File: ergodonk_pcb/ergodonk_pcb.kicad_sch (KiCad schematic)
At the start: 133 parts, among them J10 TRRS Double Sided, J12 Conn_01x04_Socket, Q1 TIP120, SW08_RH10 SW_PUSH_LED, SW1 SW_PUSH_LED, SW10 SW_PUSH_LED, SW11 SW_PUSH_LED, SW12 SW_PUSH_LED, SW13 SW_PUSH_LED, SW14 SW_PUSH_LED, SW15 SW_PUSH_LED, SW16 SW_PUSH_LED, SW17 SW_PUSH_LED, SW18_RH10 SW_PUSH_LED, SW2 SW_PUSH_LED, SW20 SW_PUSH_LED, SW21 SW_PUSH_LED, SW22 SW_PUSH_LED, SW23 SW_PUSH_LED, SW24 SW_PUSH_LED, SW25 SW_PUSH_LED, SW26 SW_PUSH_LED, SW27 SW_PUSH_LED, SW28_RH10 SW_PUSH_LED, SW3 SW_PUSH_LED, SW30 SW_PUSH_LED, SW31 SW_PUSH_LED, SW32 SW_PUSH_LED, SW33 SW_PUSH_LED, SW34 SW_PUSH_LED, SW35 SW_PUSH_LED, SW36 SW_PUSH_LED, SW37 SW_PUSH_LED, SW38_RH10 SW_PUSH_LED, SW4 SW_PUSH_LED, SW40 SW_PUSH_LED, SW42 SW_PUSH_LED, SW43 SW_PUSH_LED, SW44 SW_PUSH_LED, SW45 SW_PUSH_LED, SW46 SW_PUSH_LED, SW47 SW_PUSH_LED, SW48_RH10 SW_PUSH_LED, SW5 SW_PUSH_LED, SW50 SW_PUSH_LED, SW51 SW_PUSH_LED, SW52 SW_PUSH_LED, SW53 SW_PUSH_LED, SW54 SW_PUSH_LED, SW55 SW_PUSH_LED, SW56 SW_PUSH_LED, SW57 SW_PUSH_LED, SW58 SW_PUSH_LED, SW6 SW_PUSH_LED, SW7 SW_PUSH_LED, U10 Pico

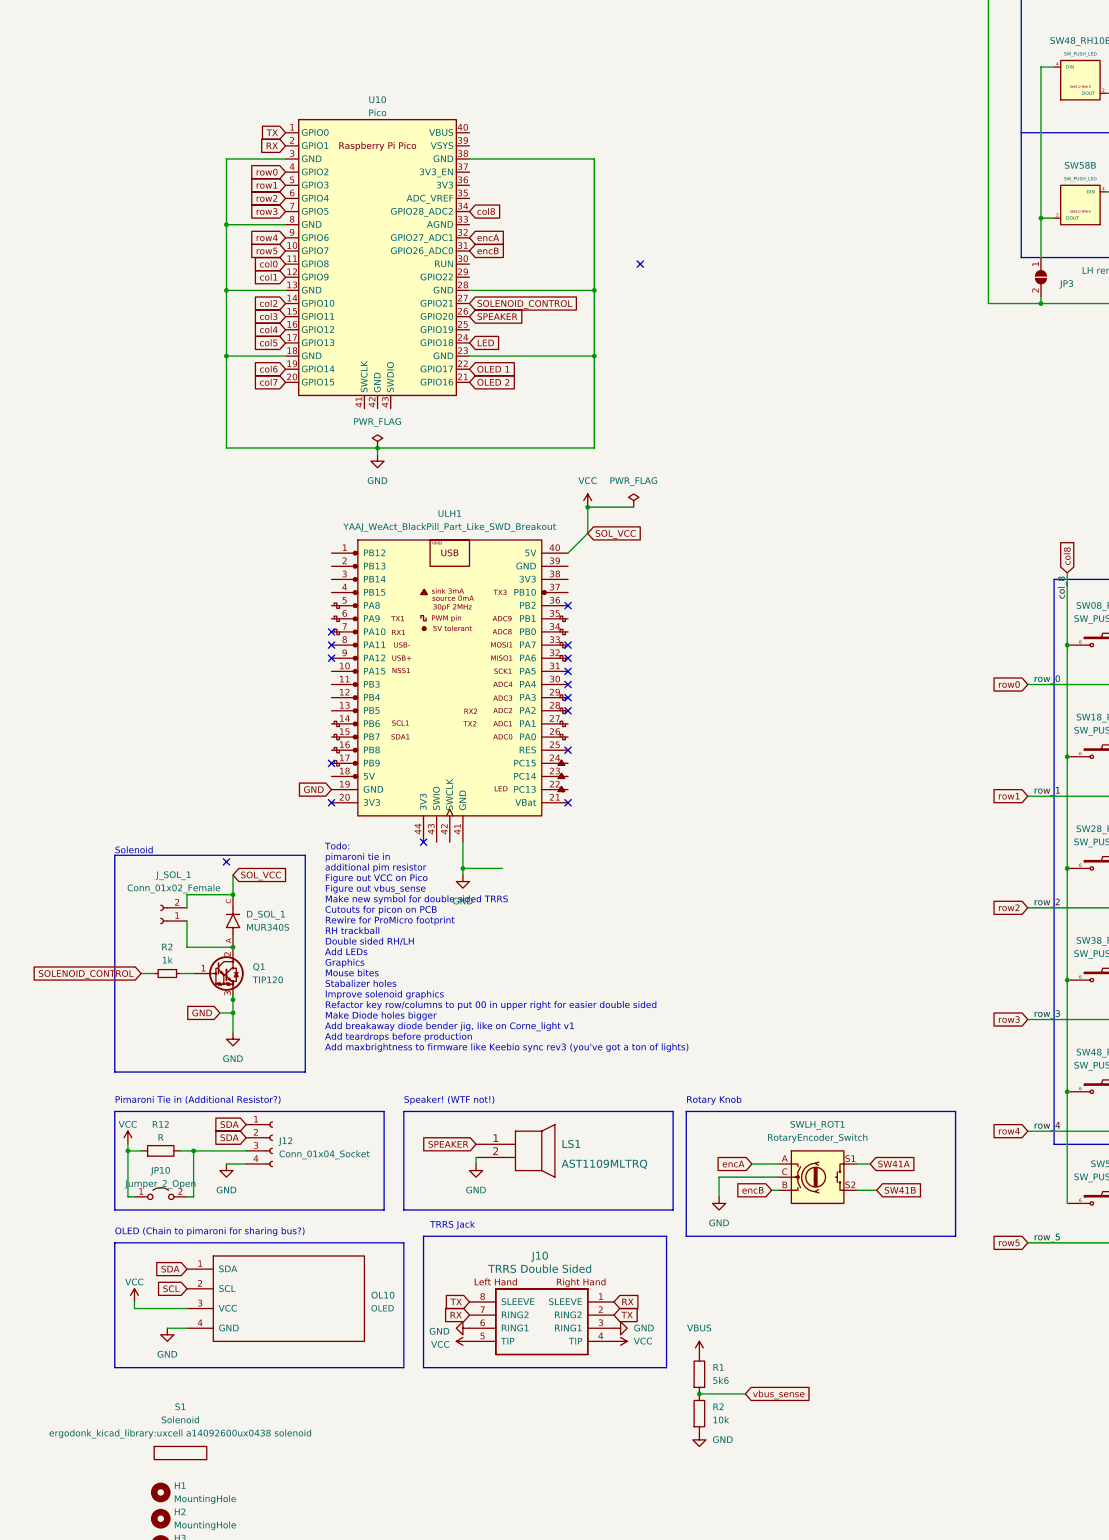
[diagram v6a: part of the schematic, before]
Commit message: Removed blackpill from schematic and pcb Updated pico placement Updated outline source for Inkscape regeneration
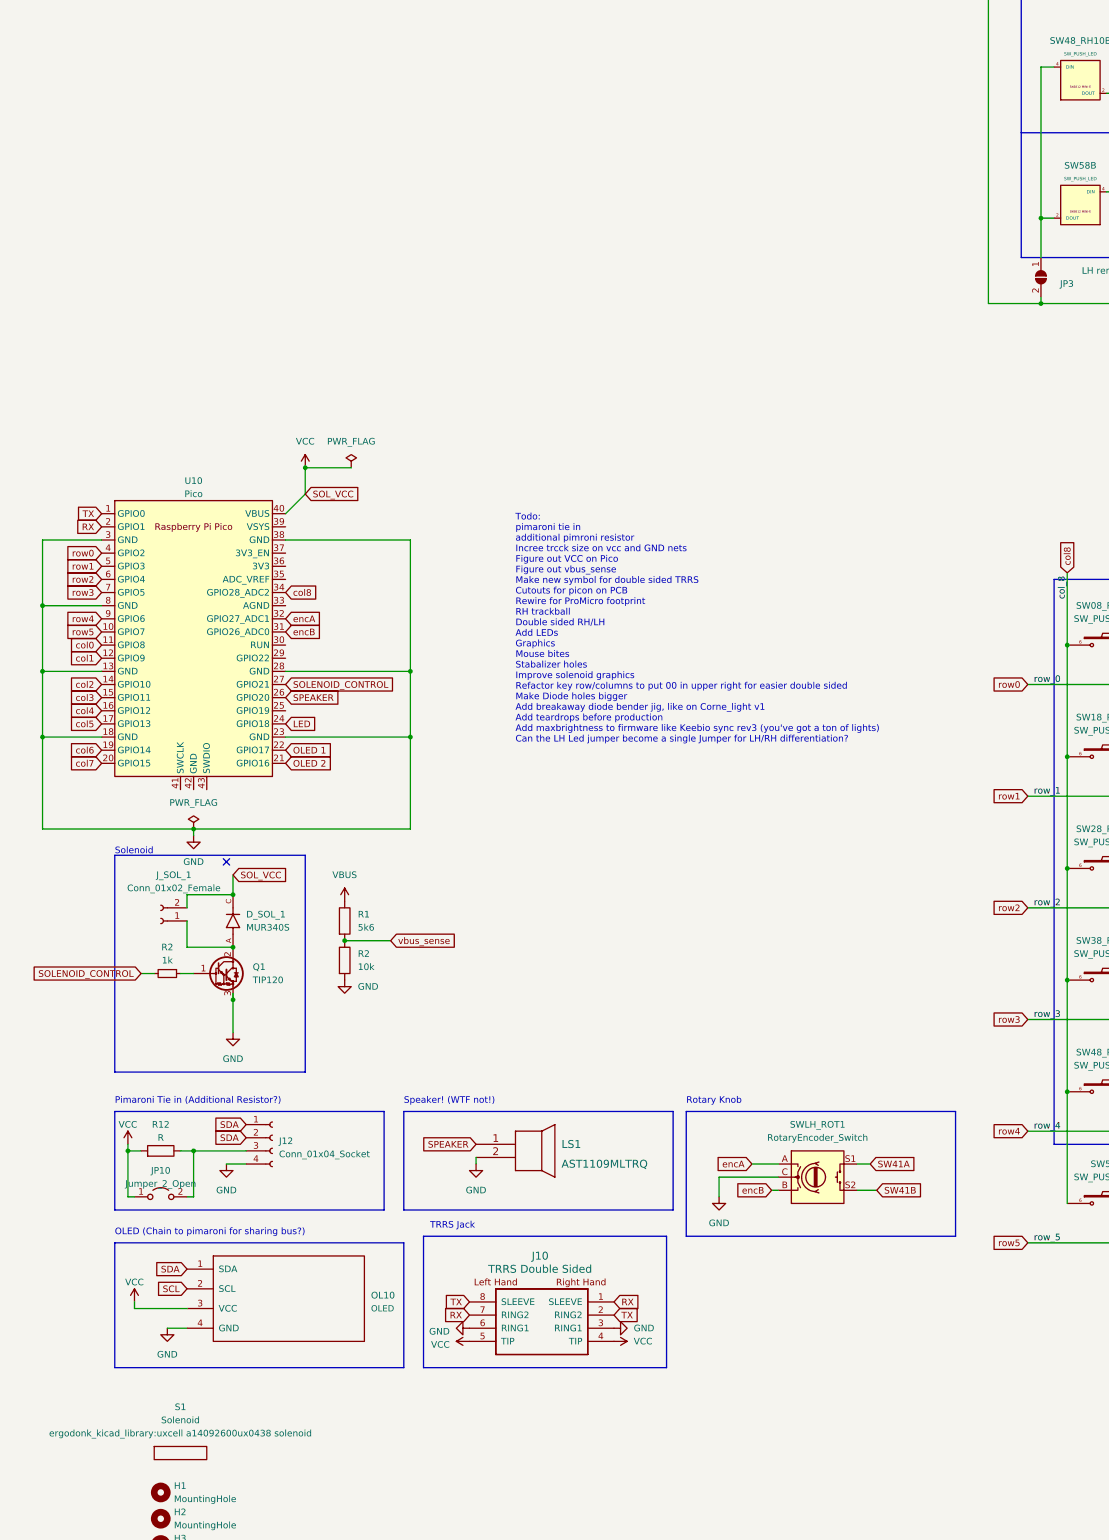
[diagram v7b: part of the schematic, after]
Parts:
- removed ULH1: YAAJ_WeAct_BlackPill_Part_Like_SWD_Breakout, Footprints:YAAJ_WeAct_BlackPill_SWD_2, symbol YAAJ_WeAct_BlackPill_Part_Like_SWD_Breakout:YAAJ_WeAct_BlackPill_Part_Like_SWD_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
- U10: footprint RPi_Pico:RPi_Pico_SMD_TH -> MCU_RaspberryPi_and_Boards:RPi_Pico_SMD_TH
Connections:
- net VCC: now also U10.40 (VBUS)
- no-connect marks 17 -> 1
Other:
- note added: "Todo: pimaroni tie in additional pimroni resistor Incree trcck size on vcc and GND nets Figure out VCC on Pico Figure out vbus_sense Make new symbol for double sided TRRS Cutouts for picon on PCB Rewire for ProMicro footprint RH trackball Double sided RH/LH Add LEDs Graphics Mouse bites Stabalizer holes Improve solenoid graphics Refactor key row/columns to put 00 in upper right for easier double 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"
- note removed: "Todo: pimaroni tie in additional pim resistor Figure out VCC on Pico Figure out vbus_sense Make new symbol for double sided TRRS Cutouts for picon on PCB Rewire for ProMicro footprint RH trackball Double sided RH/LH Add LEDs Graphics Mouse bites Stabalizer holes Improve solenoid graphics Refactor key row/columns to put 00 in upper right for easier double sided Make Diode holes bigger Add breakawa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"
- moved on the sheet: R1, R2, U10

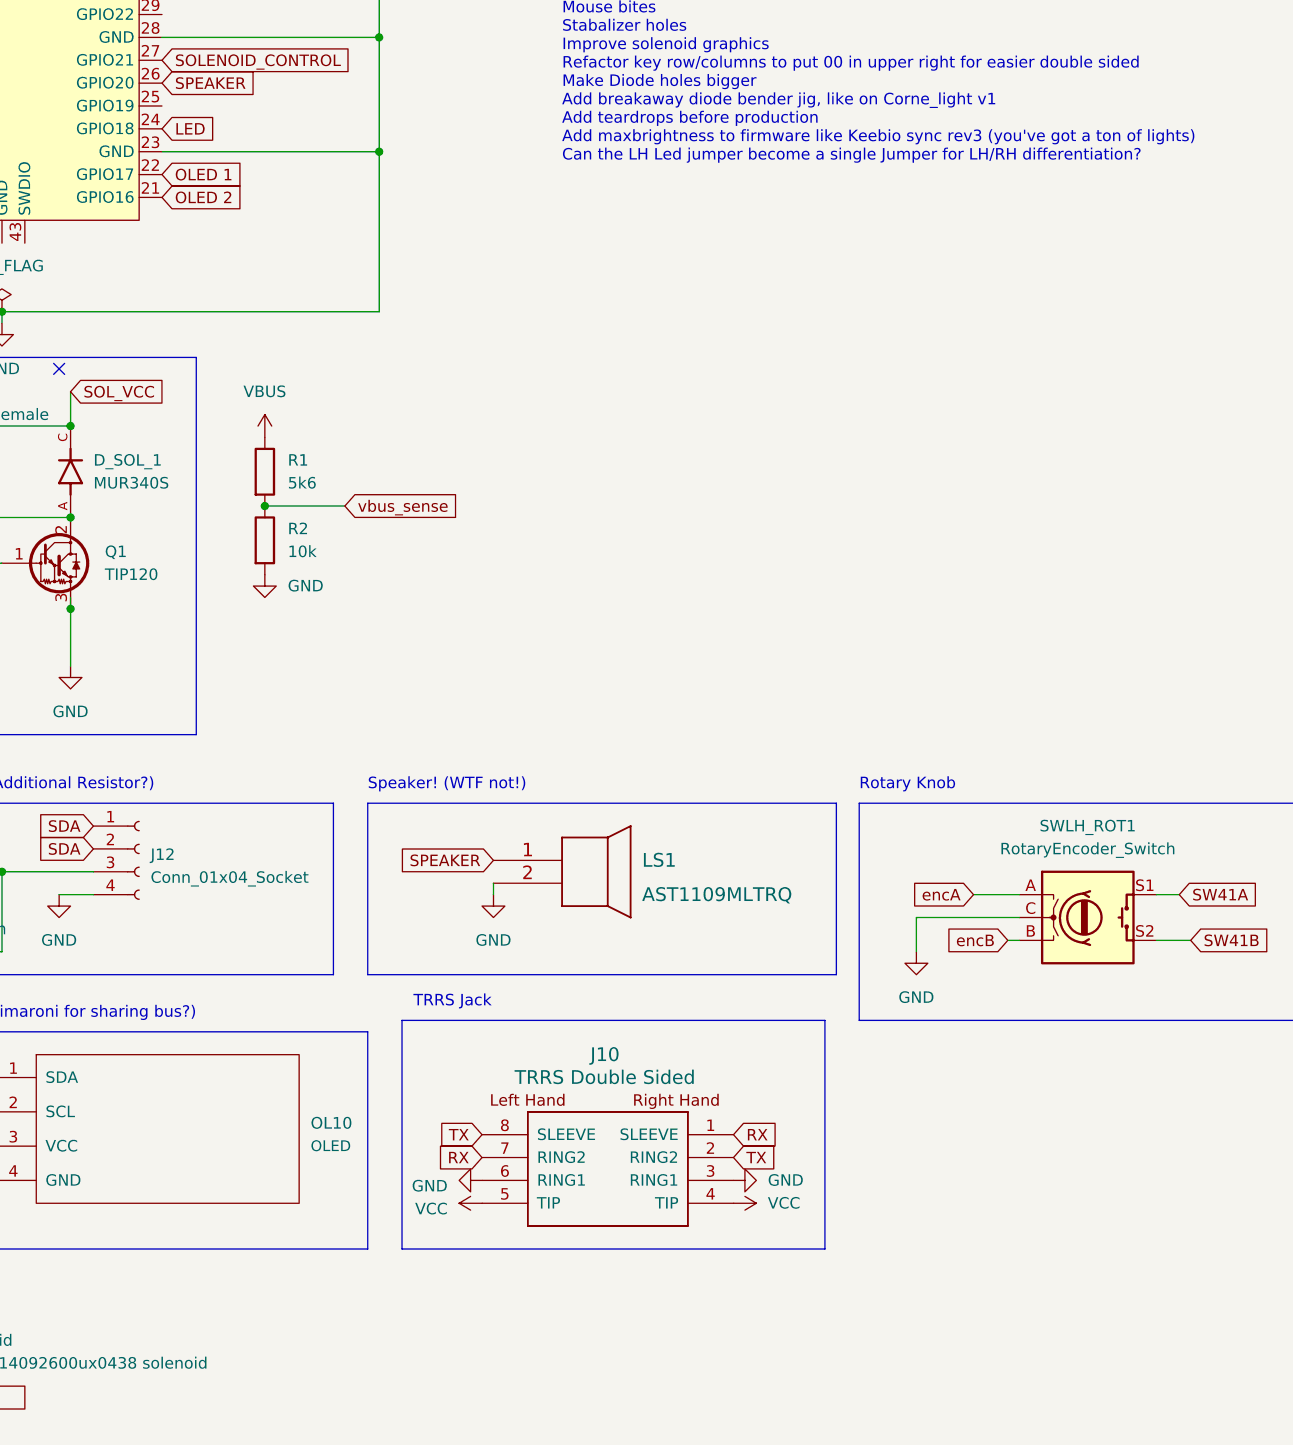
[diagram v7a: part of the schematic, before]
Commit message: Added pimaroni rough symbol
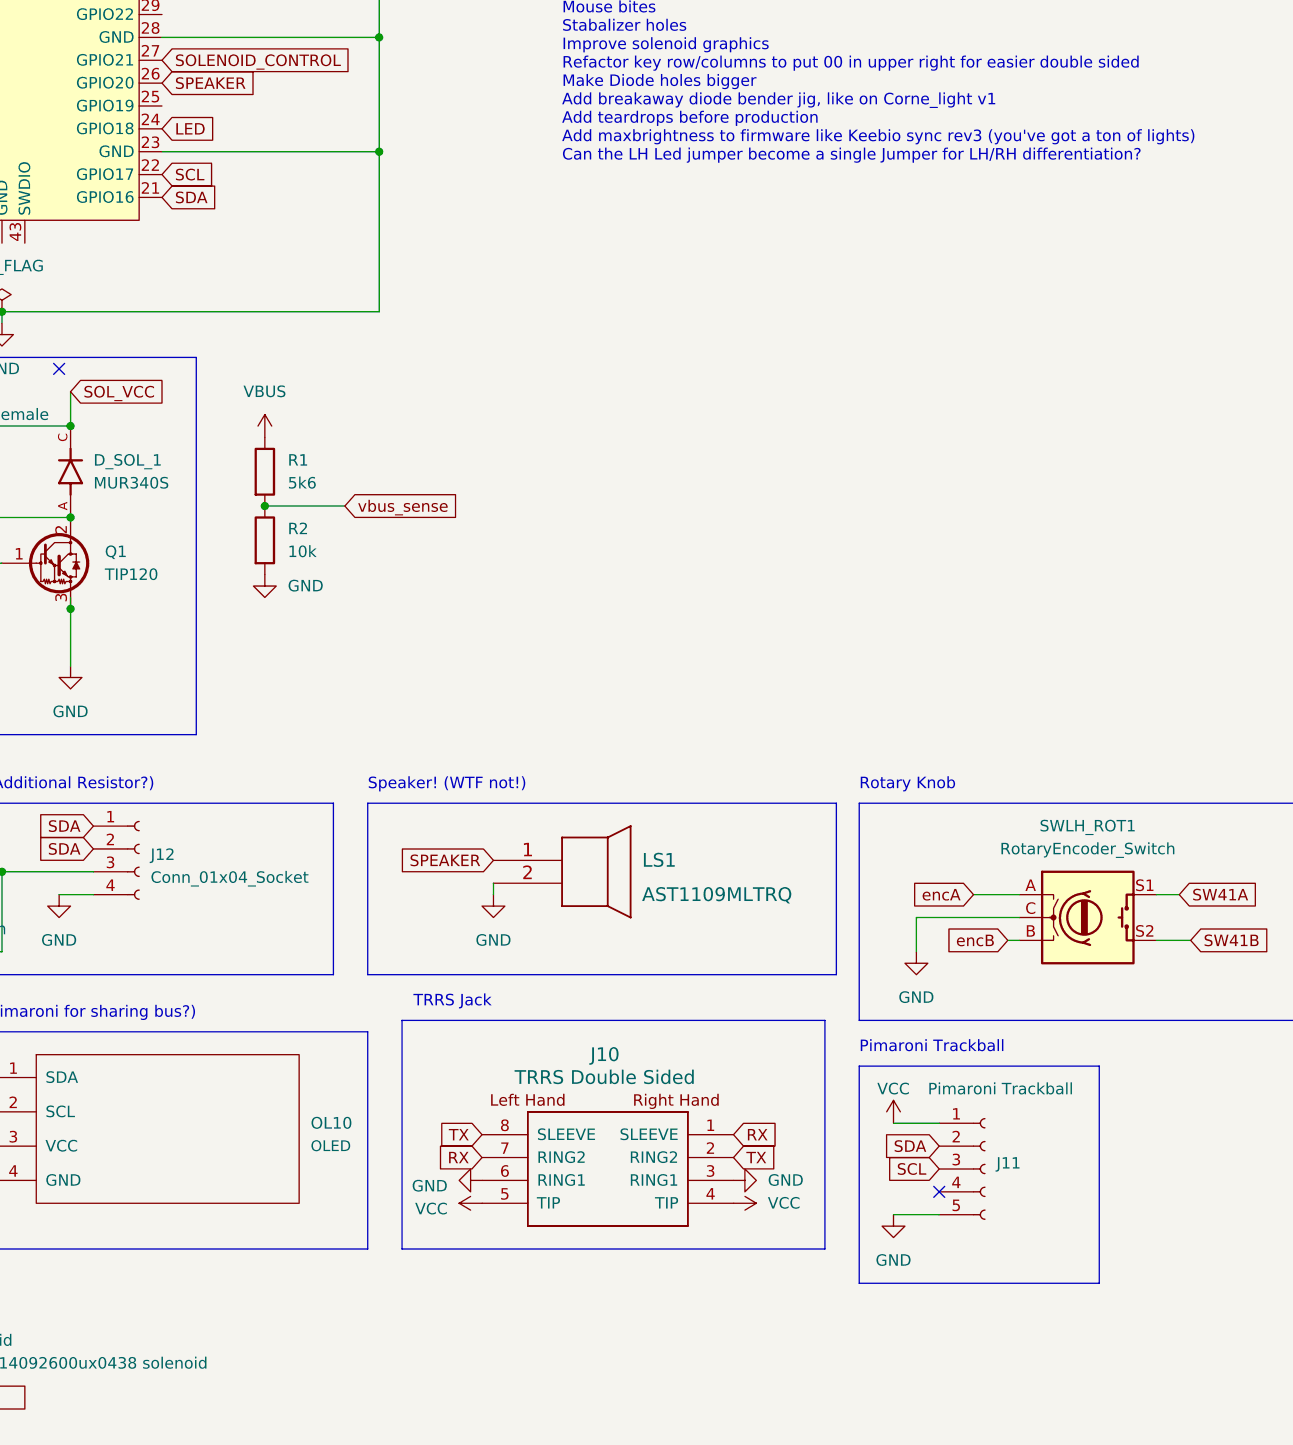
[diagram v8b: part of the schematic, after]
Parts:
- added J11: Pimaroni Trackball, ergodonk_kicad_library:pimoroni_trackball, symbol Connector:Conn_01x05_Socket
- OL10: footprint (none) -> ergodonk_kicad_library:OLED 128x64 Double sided
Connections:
- net OLED 1 is gone; now on net SCL: U10.22 (GPIO17)
- net OLED 2 is gone; now on net SDA: U10.21 (GPIO16)
- net GND: now also J11.5 (Pin_5)
- net SCL: now also J11.3 (Pin_3)
- net SDA: now also J11.2 (Pin_2)
- net VCC: now also J11.1 (Pin_1)
- no-connect marks 1 -> 2
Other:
- note added: "Pimaroni Trackball"
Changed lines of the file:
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@@
   )
   (no_connect (at 50.8 87.63))
+  (no_connect (at 148.59 179.07))
   (wire (pts (xy 50.8 146.05) (xy 54.61 146.05))
     (stroke (width 0) (type default))
@@
     (stroke (width 0) (type default))
   )
+  (wire (pts (xy 143.51 171.45) (xy 148.59 171.45))
+    (stroke (width 0) (type default))
+  )
   (wire (pts (xy 44.45 143.51) (xy 44.45 152.4))
     (stroke (width 0) (type default))
@@
     (stroke (width 0) (type default))
   )
+  (wire (pts (xy 143.51 181.61) (xy 148.59 181.61))
+    (stroke (width 0) (type default))
+  )
   (wire (pts (xy 384.81 -104.14) (xy 382.27 -104.14))
     (stroke (width 0) (type default))
@@
     (fill (type none))
   )
+  (rectangle (start 139.7 165.1) (end 166.37 189.23)
+    (stroke (width 0) (type default))
+    (fill (type none))
+  )
   (image (at 248.92 214.63) (scale 1.76046)
     (data
@@
     (effects (font (size 1.27 1.27)) (justify left bottom))
   )
+  (text "Pimaroni Trackball\n" (at 139.7 163.83 0)
+    (effects (font (size 1.27 1.27)) (justify left bottom))
+  )
   (text "Solenoid" (at 29.21 86.36 0)
     (effects (font (size 1.27 1.27)) (justify left bottom))
@@
     )
   )
+  (global_label "SCL" (shape input) (at 148.59 176.53 180) (fields_autoplaced)
+    (effects (font (size 1.27 1.27)) (justify right))
+    (property "Intersheetrefs" "${INTERSHEET_REFS}" (at 142.1766 176.53 0)
+      (effects (font (size 1.27 1.27)) (justify right) hide)
+    )
+  )
   (global_label "encB" (shape input) (at 62.23 43.18 0) (fields_autoplaced)
     (effects (font (size 1.27 1.27)) (justify left))
@@
     )
   )
+  (global_label "SDA" (shape input) (at 148.59 173.99 180) (fields_autoplaced)
+    (effects (font (size 1.27 1.27)) (justify right))
+    (property "Intersheetrefs" "${INTERSHEET_REFS}" (at 142.1161 173.99 0)
+      (effects (font (size 1.27 1.27)) (justify right) hide)
+    )
+  )
   (global_label "col5" (shape input) (at 26.67 60.96 180) (fields_autoplaced)
     (effects (font (size 1.27 1.27)) (justify right))
@@
     )
   )
-  (global_label "OLED 1" (shape input) (at 62.23 66.04 0) (fields_autoplaced)
+  (global_label "SCL" (shape input) (at 62.23 66.04 0) (fields_autoplaced)
     (effects (font (size 1.27 1.27)) (justify left))
-    (property "Intersheetrefs" "${INTERSHEET_REFS}" (at 71.8849 66.04 0)
+    (property "Intersheetrefs" "${INTERSHEET_REFS}" (at 68.6434 66.04 0)
       (effects (font (size 1.27 1.27)) (justify left) hide)
     )
@@
     )
   )
-  (global_label "OLED 2" (shape input) (at 62.23 68.58 0) (fields_autoplaced)
+  (global_label "SDA" (shape input) (at 62.23 68.58 0) (fields_autoplaced)
     (effects (font (size 1.27 1.27)) (justify left))
-    (property "Intersheetrefs" "${INTERSHEET_REFS}" (at 71.8849 68.58 0)
+    (property "Intersheetrefs" "${INTERSHEET_REFS}" (at 68.7039 68.58 0)
       (effects (font (size 1.27 1.27)) (justify left) hide)
     )
@@
     )
   )
+  (symbol (lib_name "VCC_1") (lib_id "power:VCC") (at 143.51 171.45 0) (unit 1)
+    (in_bom yes) (on_board yes) (dnp no)
+    (property "Reference" "#PWR022" (at 143.51 175.26 0)
+      (effects (font (size 1.27 1.27)) hide)
+    )
+    (property "Value" "VCC" (at 143.51 167.64 0)
+      (effects (font (size 1.27 1.27)))
+    )
+    (property "Footprint" "" (at 143.51 171.45 0)
+      (effects (font (size 1.27 1.27)) hide)
+    )
+    (property "Datasheet" "" (at 143.51 171.45 0)
+      (effects (font (size 1.27 1.27)) hide)
+    )
+    (pin "1")
+    (instances
+      (project "ergodonk_pcb"
+        (path "/ed1aaf15-4e1f-4159-b371-d99b3fb972ad"
+          (reference "#PWR022") (unit 1)
+        )
+      )
+    )
+  )
   (symbol (lib_id "SofleKeyboard:SW_PUSH_LED") (at 215.9 -63.5 0) (mirror y) (unit 2)
     (in_bom yes) (on_board yes) (dnp no)
@@
     )
   )
+  (symbol (lib_id "Connector:Conn_01x05_Socket") (at 153.67 176.53 0) (unit 1)
+    (in_bom yes) (on_board yes) (dnp no)
+    (property "Reference" "J11" (at 154.94 175.895 0)
+      (effects (font (size 1.27 1.27)) (justify left))
+    )
+    (property "Value" "Pimaroni Trackball" (at 147.32 167.64 0)
+      (effects (font (size 1.27 1.27)) (justify left))
+    )
+    (property "Footprint" "ergodonk_kicad_library:pimoroni_trackball" (at 153.67 176.53 0)
+      (effects (font (size 1.27 1.27)) hide)
+    )
+    (property "Datasheet" "~" (at 153.67 176.53 0)
+      (effects (font (size 1.27 1.27)) hide)
+    )
+    (pin "1")
+    (pin "2")
+    (pin "3")
+    (pin "4")
+    (pin "5")
+    (instances
+      (project "ergodonk_pcb"
+        (path "/ed1aaf15-4e1f-4159-b371-d99b3fb972ad"
+          (reference "J11") (unit 1)
+        )
+      )
+    )
+  )
   (symbol (lib_id "SofleKeyboard:SW_PUSH_LED") (at 220.98 45.72 0) (unit 1)
     (in_bom yes) (on_board yes) (dnp no) (fields_autoplaced)
@@
     )
   )
+  (symbol (lib_name "GND_1") (lib_id "power:GND") (at 143.51 181.61 0) (unit 1)
+    (in_bom yes) (on_board yes) (dnp no) (fields_autoplaced)
+    (property "Reference" "#PWR023" (at 143.51 187.96 0)
+      (effects (font (size 1.27 1.27)) hide)
+    )
+    (property "Value" "GND" (at 143.51 186.69 0)
+      (effects (font (size 1.27 1.27)))
+    )
+    (property "Footprint" "" (at 143.51 181.61 0)
+      (effects (font (size 1.27 1.27)) hide)
+    )
+    (property "Datasheet" "" (at 143.51 181.61 0)
+      (effects (font (size 1.27 1.27)) hide)
+    )
+    (pin "1")
+    (instances
+      (project "ergodonk_pcb"
+        (path "/ed1aaf15-4e1f-4159-b371-d99b3fb972ad"
+          (reference "#PWR023") (unit 1)
+        )
+      )
+    )
+  )
   (symbol (lib_id "SofleKeyboard:SW_PUSH_LED") (at 307.34 153.67 0) (unit 1)
     (in_bom yes) (on_board yes) (dnp no) (fields_autoplaced)
@@
       (effects (font (size 1.1938 1.1938)) (justify left))
     )
-    (property "Footprint" "" (at 62.23 170.18 0)
+    (property "Footprint" "ergodonk_kicad_library:OLED 128x64 Double sided" (at 62.23 170.18 0)
       (effects (font (size 1.524 1.524)) hide)
     )
